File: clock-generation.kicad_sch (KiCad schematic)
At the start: 0 parts

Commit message: wip
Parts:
- added U1: Si5351B-B-GM, Package_DFN_QFN:QFN-20-1EP_4x4mm_P0.5mm_EP2.7x2.7mm, symbol Oscillator:Si5351B-B-GM
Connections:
- new net SCL: U1.4 (SCL)
- new net SDA: U1.5 (SDA)
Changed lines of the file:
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@@
 	(generator_version "8.0")
 	(paper "A4")
+	(wire
+		(pts
+			(xy 92.71 83.82) (xy 121.92 83.82)
+		)
+		(stroke
+			(width 0)
+			(type default)
+		)
+	)
+	(wire
+		(pts
+			(xy 92.71 86.36) (xy 121.92 86.36)
+		)
+		(stroke
+			(width 0)
+			(type default)
+		)
+	)
+	(hierarchical_label "SCL"
+		(shape bidirectional)
+		(at 92.71 86.36 180)
+		(fields_autoplaced yes)
+		(effects
+			(font
+				(size 1.27 1.27)
+			)
+			(justify right)
+		)
+	)
+	(hierarchical_label "SDA"
+		(shape bidirectional)
+		(at 92.71 83.82 180)
+		(fields_autoplaced yes)
+		(effects
+			(font
+				(size 1.27 1.27)
+			)
+			(justify right)
+		)
+	)
+	(symbol
+		(lib_id "Oscillator:Si5351B-B-GM")
+		(at 137.16 78.74 0)
+		(unit 1)
+		(exclude_from_sim no)
+		(in_bom yes)
+		(on_board yes)
+		(dnp no)
+		(fields_autoplaced yes)
+		(property "Reference" "U1"
+			(at 139.3541 101.6 0)
+			(effects
+				(font
+					(size 1.27 1.27)
+				)
+				(justify left)
+			)
+		)
+		(property "Value" "Si5351B-B-GM"
+			(at 139.3541 104.14 0)
+			(effects
+				(font
+					(size 1.27 1.27)
+				)
+				(justify left)
+			)
+		)
+		(property "Footprint" "Package_DFN_QFN:QFN-20-1EP_4x4mm_P0.5mm_EP2.7x2.7mm"
+			(at 137.16 109.22 0)
+			(effects
+				(font
+					(size 1.27 1.27)
+				)
+				(hide yes)
+			)
+		)
+		(property "Datasheet" "https://www.silabs.com/documents/public/data-sheets/Si5351-B.pdf"
+			(at 137.16 78.74 0)
+			(effects
+				(font
+					(size 1.27 1.27)
+				)
+				(hide yes)
+			)
+		)
+		(property "Description" "I2C Programmable Any-Frequency CMOS Clock Generator + VCXO, QFN-20"
+			(at 137.16 78.74 0)
+			(effects
+				(font
+					(size 1.27 1.27)
+				)
+				(hide yes)
+			)
+		)
+		(pin "17"
+		)
+		(pin "21"
+		)
+		(pin "20"
+		)
+		(pin "2"
+		)
+		(pin "3"
+		)
+		(pin "9"
+		)
+		(pin "1"
+		)
+		(pin "13"
+		)
+		(pin "5"
+		)
+		(pin "7"
+		)
+		(pin "4"
+		)
+		(pin "6"
+		)
+		(pin "15"
+		)
+		(pin "10"
+		)
+		(pin "8"
+		)
+		(pin "14"
+		)
+		(pin "18"
+		)
+		(pin "11"
+		)
+		(pin "16"
+		)
+		(pin "12"
+		)
+		(pin "19"
+		)
+		(instances
+			(project ""
+				(path "/df100556-b288-4cb1-b69f-c0734132cb90/be7c4f40-c0c2-47f2-9c0c-8904af6555df"
+					(reference "U1")
+					(unit 1)
+				)
+			)
+		)
+	)
 )

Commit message: wip
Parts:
- added U2: TPS79301-EP, Package_TO_SOT_SMD:SOT-23-6, symbol Regulator_Linear:TPS79301-EP
- added U3: ~, symbol dante-audio-board:DAC53002
- added Y1: 7M-27.000MEEQ-T, Crystal:Crystal_SMD_TXC_7M-4Pin_3.2x2.5mm, symbol Device:Crystal_GND24
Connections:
- net at U1.1 (XA): now also Y1.3
- net OSC_LRCLK: now reaches U1.12 (CLK1)
- net OSC_SCLK: now reaches U1.13 (CLK0)
- net at U1.2 (XB): now also Y1.1
- net GND: now reaches U1.21 (GND)
- net GND: now also U1.6 (SSEN), U1.7 (OEB), U3.14 (AGND), Y1.2, Y1.4
- net COUNTER_FB: now reaches U1.8 (CLK3)
- net OSC_MCLK: now reaches U1.9 (CLK2)
- no-connect marks 0 -> 4
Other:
- moved on the sheet: U1

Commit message: add more CI steps
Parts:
- U3: footprint (none) -> dante-audio-board:IC_BQ25306RTER
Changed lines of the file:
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@@
 			)
 		)
-		(property "Footprint" ""
+		(property "Footprint" "dante-audio-board:IC_BQ25306RTER"
 			(at 63.5 57.15 0)
 			(effects

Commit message: rename everything
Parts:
- U3: footprint dante-audio-board:IC_BQ25306RTER -> Library:IC_BQ25306RTER; symbol dante-audio-board:DAC53002 -> jkembedded-audio-board:DAC53002
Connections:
- net GND: no longer U3.14 (AGND)
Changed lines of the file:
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@@
 	)
 	(symbol
-		(lib_id "dante-audio-board:DAC53002")
+		(lib_id "jkembedded-audio-board:DAC53002")
 		(at 63.5 57.15 0)
 		(unit 1)
@@
 			)
 		)
-		(property "Footprint" "dante-audio-board:IC_BQ25306RTER"
+		(property "Footprint" "Library:IC_BQ25306RTER"
 			(at 63.5 57.15 0)
 			(effects

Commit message: fix DAC53002 path in clock-generation schematic
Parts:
- U3: symbol jkembedded-audio-board:DAC53002 -> Library:DAC53002
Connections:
- net GND: now also U3.14 (AGND)
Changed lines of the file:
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@@
 	)
 	(symbol
-		(lib_id "jkembedded-audio-board:DAC53002")
+		(lib_id "Library:DAC53002")
 		(at 63.5 57.15 0)
 		(unit 1)

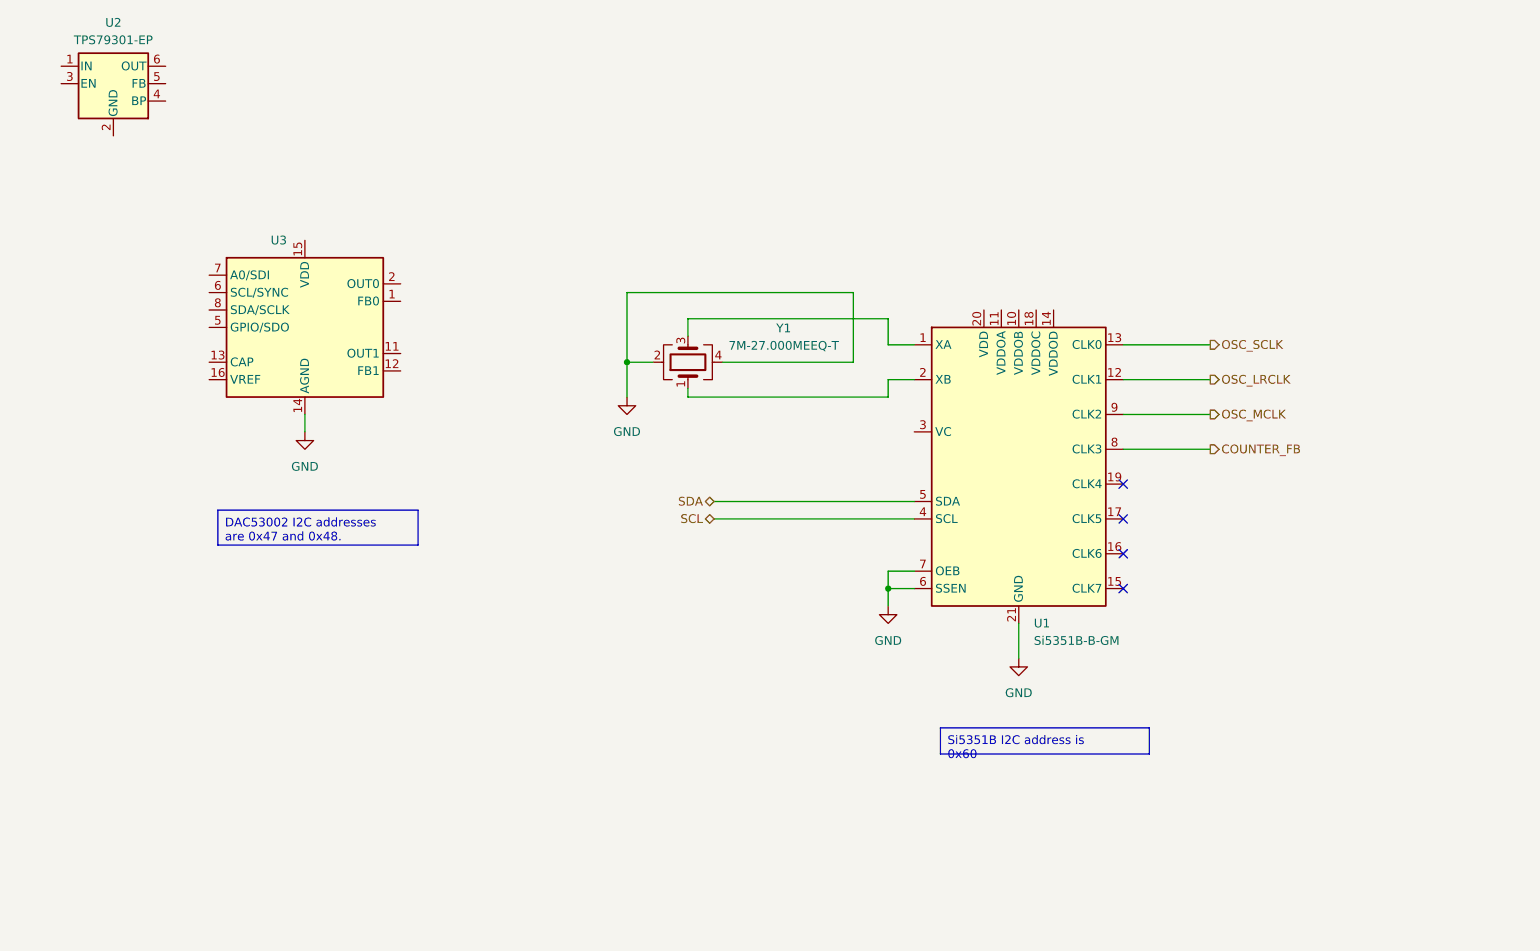
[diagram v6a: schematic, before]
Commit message: almost done with clocking, need series terminators
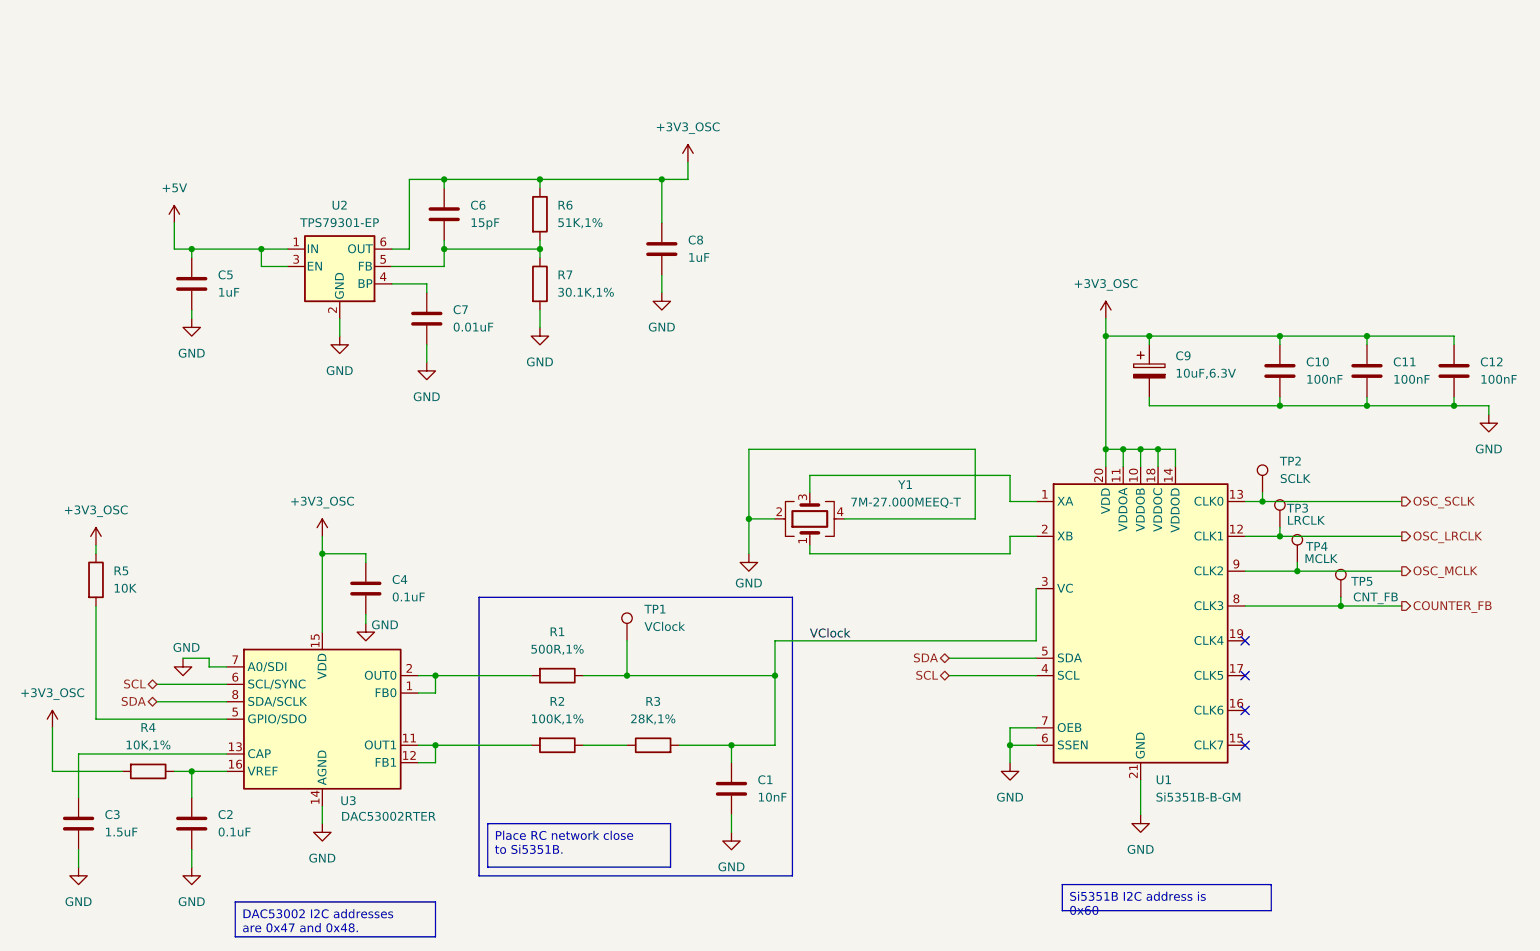
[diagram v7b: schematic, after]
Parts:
- added C1: 10nF, Capacitor_SMD:C_0603_1608Metric, symbol Device:C
- added C10, C11, C12: 100nF, Capacitor_SMD:C_0603_1608Metric, symbol Device:C
- added C2, C4: 0.1uF, Capacitor_SMD:C_0603_1608Metric, symbol Device:C
- added C3: 1.5uF, Capacitor_SMD:C_0603_1608Metric, symbol Device:C
- added C5, C8: 1uF, Capacitor_SMD:C_0603_1608Metric, symbol Device:C
- added C6: 15pF, Capacitor_SMD:C_0603_1608Metric, symbol Device:C
- added C7: 0.01uF, Capacitor_SMD:C_0603_1608Metric, symbol Device:C
- added C9: 10uF,6.3V, Capacitor_Tantalum_SMD:CP_EIA-6032-15_Kemet-U, symbol Device:C_Polarized
- added R1: 500R,1%, Resistor_SMD:R_0603_1608Metric, symbol Device:R
- added R2: 100K,1%, Resistor_SMD:R_0603_1608Metric, symbol Device:R
- added R3: 28K,1%, Resistor_SMD:R_0603_1608Metric, symbol Device:R
- added R4: 10K,1%, Resistor_SMD:R_0603_1608Metric, symbol Device:R
- added R5: 10K, Resistor_SMD:R_0603_1608Metric, symbol Device:R
- added R6: 51K,1%, Resistor_SMD:R_0603_1608Metric, symbol Device:R
- added R7: 30.1K,1%, Resistor_SMD:R_0603_1608Metric, symbol Device:R
- added TP1: VClock, TestPoint:TestPoint_Pad_D1.0mm, symbol Connector:TestPoint
- added TP2: SCLK, TestPoint:TestPoint_Pad_D1.0mm, symbol Connector:TestPoint
- added TP3: LRCLK, TestPoint:TestPoint_Pad_D1.0mm, symbol Connector:TestPoint
- added TP4: MCLK, TestPoint:TestPoint_Pad_D1.0mm, symbol Connector:TestPoint
- added TP5: CNT_FB, TestPoint:TestPoint_Pad_D1.0mm, symbol Connector:TestPoint
- U3: value ~ -> DAC53002RTER
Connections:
- net COUNTER_FB: now also TP5.1
- net GND: now also U2.2 (GND), U3.7 (A0/SDI), C1.2, C10.2, C11.2, C12.2, C2.2, C3.2, C4.2, C5.2, C7.2, C8.2, C9.2, R7.2
- net OSC_LRCLK: now also TP3.1
- net OSC_MCLK: now also TP4.1
- net OSC_SCLK: now also TP2.1
- net SCL: now also U3.6 (SCL/SYNC)
- net SDA: now also U3.8 (SDA/SCLK)
- net at U3.1 (FB0): now also U3.2 (OUT0), R1.2
- net at U3.11 (OUT1): now also U3.12 (FB1), R2.2
- net at U3.13 (CAP): now also C3.1
- net +3V3_OSC: now reaches U3.15 (VDD)
- net +3V3_OSC: now also U1.10 (VDDOB), U1.11 (VDDOA), U1.14 (VDDOD), U1.18 (VDDOC), U1.20 (VDD), U2.6 (OUT), C10.1, C11.1, C12.1, C4.1, C6.1, C8.1, C9.1, R4.2, R5.1, R6.1
- net at U3.16 (VREF): now also C2.1, R4.1
- net at U3.5 (GPIO/SDO): now also R5.2
- net +5V: now reaches U2.1 (IN)
- net +5V: now also U2.3 (EN), C5.1
- net at U2.4 (BP): now also C7.1
- net at U2.5 (FB): now also C6.2, R6.2, R7.1
- net VClock: now reaches U1.3 (VC)
- net VClock: now also C1.1, R1.1, R3.2, TP1.1
- new net: R2.1, R3.1
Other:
- moved on the sheet: U1, U2, U3, Y1

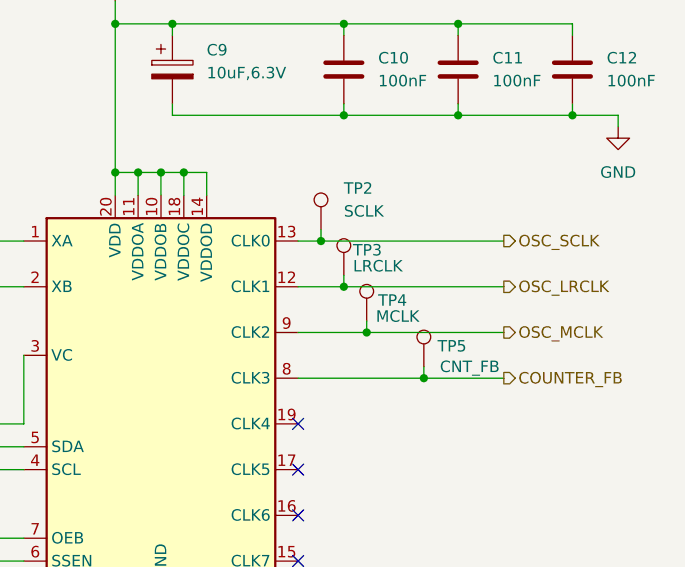
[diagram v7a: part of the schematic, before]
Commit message: mostly done with schematic of mikrobus board
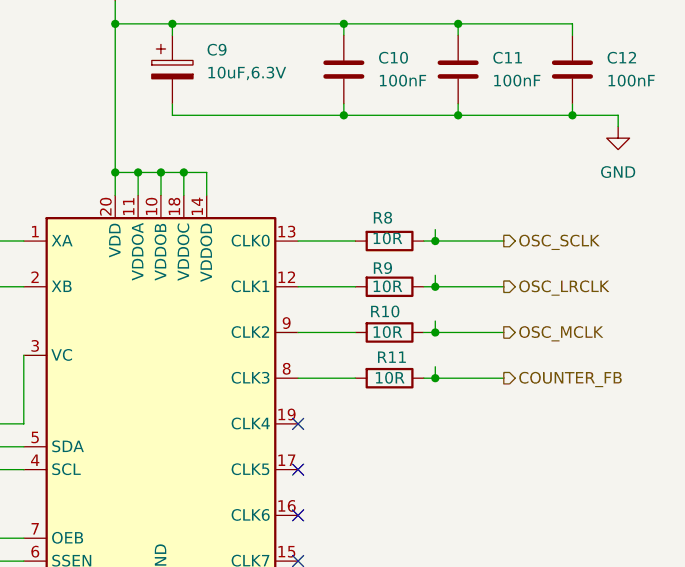
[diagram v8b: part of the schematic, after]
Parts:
- removed TP2: SCLK, TestPoint:TestPoint_Pad_D1.0mm, symbol Connector:TestPoint
- removed TP3: LRCLK, TestPoint:TestPoint_Pad_D1.0mm, symbol Connector:TestPoint
- removed TP4: MCLK, TestPoint:TestPoint_Pad_D1.0mm, symbol Connector:TestPoint
- removed TP5: CNT_FB, TestPoint:TestPoint_Pad_D1.0mm, symbol Connector:TestPoint
- added R10, R11, R8, R9: 10R, Resistor_SMD:R_0402_1005Metric, symbol Device:R
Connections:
- net COUNTER_FB: now also R11.1; no longer U1.8 (CLK3)
- net OSC_LRCLK: now also R9.1; no longer U1.12 (CLK1)
- net OSC_MCLK: now also R10.1; no longer U1.9 (CLK2)
- net OSC_SCLK: now also R8.1; no longer U1.13 (CLK0)
- new net: R11.2, U1.8 (CLK3)
- new net: R9.2, U1.12 (CLK1)
- new net: R10.2, U1.9 (CLK2)
- new net: R8.2, U1.13 (CLK0)
